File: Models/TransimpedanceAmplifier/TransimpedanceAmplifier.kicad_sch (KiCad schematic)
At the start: 1 part, among them U1 Teensy4.1

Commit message: Filled in some detail
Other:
- removed sheet TIA_1Stage
- removed sheet TIA_2Stage
- added sheet TIA_OneStage (TIA_OneStage.kicad_sch)
- added sheet TIA_TwoStage (TIA_TwoStage.kicad_sch)
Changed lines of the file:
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@@
+	)
+	(sheet
+		(at 233.68 60.96)
+		(size 35.56 25.4)
+		(exclude_from_sim no)
+		(in_bom yes)
+		(on_board yes)
+		(dnp no)
+		(fields_autoplaced yes)
+		(stroke
+			(width 0.1524)
+			(type solid)
+		)
+		(fill
+			(color 0 0 0 0.0000)
+		)
+		(property "Sheetname" "TIA_TwoStage"
+			(at 233.68 60.2484 0)
+			(effects
+				(font
+					(size 1.27 1.27)
+				)
+				(justify left bottom)
+			)
+		)
+		(property "Sheetfile" "TIA_TwoStage.kicad_sch"
+			(at 233.68 86.9446 0)
+			(effects
+				(font
+					(size 1.27 1.27)
+				)
+				(justify left top)
+			)
+		)
+		(instances
+			(project "TransimpedanceAmplifier"
+				(path "/ec9f2ae3-e40d-40eb-9760-2b611ee8efd1"
+					(page "7")
+				)
+			)
+		)
 	)
 	(sheet
@@
 	)
 	(sheet
-		(at 231.14 25.4)
-		(size 35.56 25.4)
-		(exclude_from_sim no)
-		(in_bom yes)
-		(on_board yes)
-		(dnp no)
-		(fields_autoplaced yes)
-		(stroke
-			(width 0.1524)
-			(type solid)
-		)
-		(fill
-			(color 0 0 0 0.0000)
-		)
-		(property "Sheetname" "TIA_1Stage"
-			(at 231.14 24.6884 0)
-			(effects
-				(font
-					(size 1.27 1.27)
-				)
-				(justify left bottom)
-			)
-		)
-		(property "Sheetfile" "TIA_1Stage.kicad_sch"
-			(at 231.14 51.3846 0)
-			(effects
-				(font
-					(size 1.27 1.27)
-				)
-				(justify left top)
-			)
-		)
-		(instances
-			(project "TransimpedanceAmplifier"
-				(path "/ec9f2ae3-e40d-40eb-9760-2b611ee8efd1"
-					(page "6")
-				)
-			)
-		)
-	)
-	(sheet
-		(at 231.14 63.5)
-		(size 35.56 22.86)
-		(exclude_from_sim no)
-		(in_bom yes)
-		(on_board yes)
-		(dnp no)
-		(fields_autoplaced yes)
-		(stroke
-			(width 0.1524)
-			(type solid)
-		)
-		(fill
-			(color 0 0 0 0.0000)
-		)
-		(property "Sheetname" "TIA_2Stage"
-			(at 231.14 62.7884 0)
-			(effects
-				(font
-					(size 1.27 1.27)
-				)
-				(justify left bottom)
-			)
-		)
-		(property "Sheetfile" "TIA_2Stage.kicad_sch"
-			(at 231.14 86.9446 0)
-			(effects
-				(font
-					(size 1.27 1.27)
-				)
-				(justify left top)
-			)
-		)
-		(instances
-			(project "TransimpedanceAmplifier"
-				(path "/ec9f2ae3-e40d-40eb-9760-2b611ee8efd1"
-					(page "7")
-				)
-			)
-		)
-	)
-	(sheet
 		(at 27.94 132.08)
 		(size 33.02 25.4)
@@
 				)
 			)
+		)
+	)
+	(sheet
+		(at 233.68 25.4)
+		(size 35.56 25.4)
+		(exclude_from_sim no)
+		(in_bom yes)
+		(on_board yes)
+		(dnp no)
+		(fields_autoplaced yes)
+		(stroke
+			(width 0.1524)
+			(type solid)
+		)
+		(fill
+			(color 0 0 0 0.0000)
+		)
+		(property "Sheetname" "TIA_OneStage"
+			(at 233.68 24.6884 0)
+			(effects
+				(font
+					(size 1.27 1.27)
+				)
+				(justify left bottom)
+			)
+		)
+		(property "Sheetfile" "TIA_OneStage.kicad_sch"
+			(at 233.68 51.3846 0)
+			(effects
+				(font
+					(size 1.27 1.27)
+				)
+				(justify left top)
+			)
+		)
+		(instances
+			(project "TransimpedanceAmplifier"
+				(path "/ec9f2ae3-e40d-40eb-9760-2b611ee8efd1"
+					(page "6")
+				)
+			)

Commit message: Save progress
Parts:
- removed U1: Teensy4.1, symbol teensy:Teensy4.1
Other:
- added sheet Teensy (Teensy.kicad_sch)
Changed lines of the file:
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@@
 	(generator_version "9.0")
 	(paper "A4")
-	(symbol
-		(lib_id "teensy:Teensy4.1")
-		(at 144.78 111.76 0)
-		(unit 1)
-		(exclude_from_sim no)
-		(in_bom yes)
-		(on_board yes)
-		(dnp no)
-		(fields_autoplaced yes)
-		(property "Reference" "U1"
-			(at 144.78 45.72 0)
-			(effects
-				(font
-					(size 1.27 1.27)
-				)
-			)
-		)
-		(property "Value" "Teensy4.1"
-			(at 144.78 48.26 0)
-			(effects
-				(font
-					(size 1.27 1.27)
-				)
-			)
-		)
-		(property "Footprint" ""
-			(at 134.62 101.6 0)
-			(effects
-				(font
-					(size 1.27 1.27)
-				)
-				(hide yes)
-			)
-		)
-		(property "Datasheet" ""
-			(at 134.62 101.6 0)
-			(effects
-				(font
-					(size 1.27 1.27)
-				)
-				(hide yes)
-			)
-		)
-		(property "Description" ""
-			(at 144.78 111.76 0)
-			(effects
-				(font
-					(size 1.27 1.27)
-				)
-				(hide yes)
-			)
-		)
-		(pin "5"
-		)
-		(pin "6"
-		)
-		(pin "7"
-		)
-		(pin "8"
-		)
-		(pin "9"
-		)
-		(pin "10"
-		)
-		(pin "11"
-		)
-		(pin "12"
-		)
-		(pin "13"
-		)
-		(pin "14"
-		)
-		(pin "15"
-		)
-		(pin "16"
-		)
-		(pin "17"
-		)
-		(pin "18"
-		)
-		(pin "19"
-		)
-		(pin "20"
-		)
-		(pin "21"
-		)
-		(pin "22"
-		)
-		(pin "23"
-		)
-		(pin "24"
-		)
-		(pin "66"
-		)
-		(pin "67"
-		)
-		(pin "55"
-		)
-		(pin "56"
-		)
-		(pin "57"
-		)
-		(pin "58"
-		)
-		(pin "59"
-		)
-		(pin "50"
-		)
-		(pin "51"
-		)
-		(pin "52"
-		)
-		(pin "53"
-		)
-		(pin "54"
-		)
-		(pin "49"
-		)
-		(pin "48"
-		)
-		(pin "47"
-		)
-		(pin "46"
-		)
-		(pin "45"
-		)
-		(pin "44"
-		)
-		(pin "43"
-		)
-		(pin "42"
-		)
-		(pin "41"
-		)
-		(pin "40"
-		)
-		(pin "39"
-		)
-		(pin "38"
-		)
-		(pin "37"
-		)
-		(pin "36"
-		)
-		(pin "35"
-		)
-		(pin "33"
-		)
-		(pin "32"
-		)
-		(pin "31"
-		)
-		(pin "30"
-		)
-		(pin "29"
-		)
-		(pin "28"
-		)
-		(pin "27"
-		)
-		(pin "26"
-		)
-		(pin "25"
-		)
-		(pin "65"
-		)
-		(pin "64"
-		)
-		(pin "63"
-		)
-		(pin "62"
-		)
-		(pin "61"
-		)
-		(pin "60"
-		)
-		(pin "1"
-		)
-		(pin "2"
-		)
-		(pin "3"
-		)
-		(pin "4"
-		)
-		(pin "34"
-		)
-		(instances
-			(project ""
-				(path "/ec9f2ae3-e40d-40eb-9760-2b611ee8efd1"
-					(reference "U1")
-					(unit 1)
-				)
-			)
-		)
-	)
 	(sheet
 		(at 233.68 60.96)
@@
 				)
 			)
+		)
+	)
+	(sheet
+		(at 233.68 96.52)
+		(size 35.56 25.4)
+		(exclude_from_sim no)
+		(in_bom yes)
+		(on_board yes)
+		(dnp no)
+		(fields_autoplaced yes)
+		(stroke
+			(width 0.1524)
+			(type solid)
+		)
+		(fill
+			(color 0 0 0 0.0000)
+		)
+		(property "Sheetname" "Teensy"
+			(at 233.68 95.8084 0)
+			(effects
+				(font
+					(size 1.27 1.27)
+				)
+				(justify left bottom)
+			)
+		)
+		(property "Sheetfile" "Teensy.kicad_sch"
+			(at 233.68 122.5046 0)
+			(effects
+				(font
+					(size 1.27 1.27)
+				)
+				(justify left top)
+			)
+		)
+		(instances
+			(project "TransimpedanceAmplifier"
+				(path "/ec9f2ae3-e40d-40eb-9760-2b611ee8efd1"
+					(page "10")
+				)
+			)

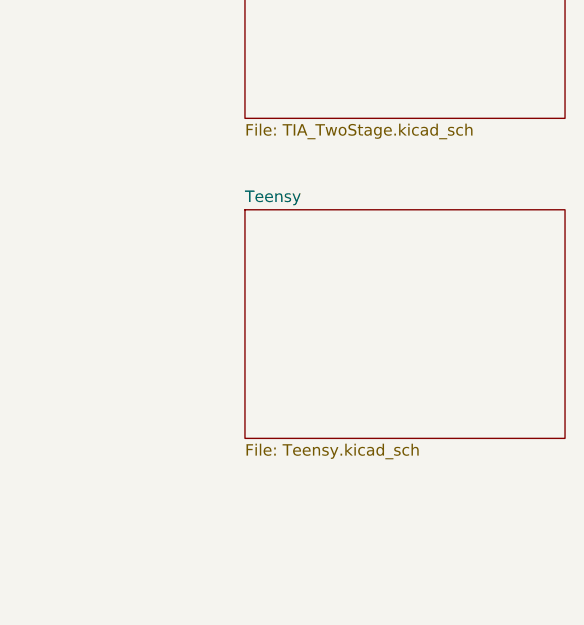
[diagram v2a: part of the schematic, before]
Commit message: Assigned all the SPI pins
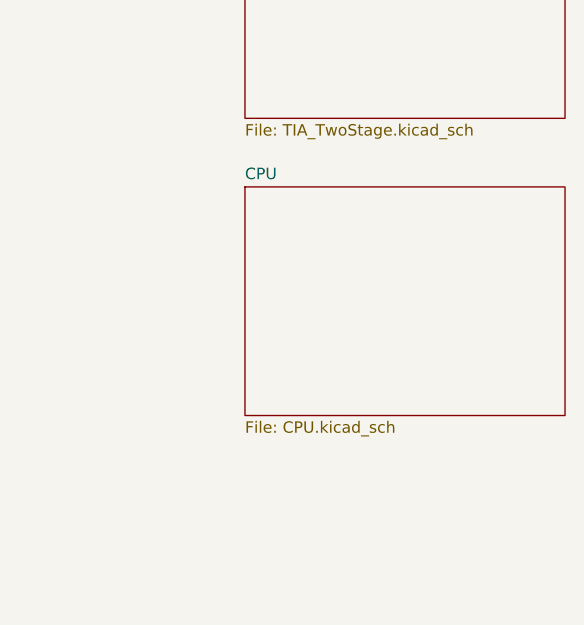
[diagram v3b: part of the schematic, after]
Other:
- removed sheet Teensy
- added sheet CPU (CPU.kicad_sch)
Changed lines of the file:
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@@
 	)
 	(sheet
-		(at 233.68 96.52)
+		(at 233.68 93.98)
 		(size 35.56 25.4)
 		(exclude_from_sim no)
@@
 			(color 0 0 0 0.0000)
 		)
-		(property "Sheetname" "Teensy"
-			(at 233.68 95.8084 0)
+		(property "Sheetname" "CPU"
+			(at 233.68 93.2684 0)
 			(effects
 				(font
@@
 			)
 		)
-		(property "Sheetfile" "Teensy.kicad_sch"
-			(at 233.68 122.5046 0)
+		(property "Sheetfile" "CPU.kicad_sch"
+			(at 233.68 119.9646 0)
 			(effects
 				(font
@@
 			(project "TransimpedanceAmplifier"
 				(path "/ec9f2ae3-e40d-40eb-9760-2b611ee8efd1"
-					(page "10")
+					(page "16")
 				)
 			)

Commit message: Save progress
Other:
- note added: "Mechanical switch to choose which TIA the current goes to and/or which TIA output voltage is read by the ADC. Unknown how this would be implemented (perhaps swapping out entire circuit boards?) Abstract away the DUT + TIA1 + TIA2 into a hierarchical sheet that just accepts input and output voltage."
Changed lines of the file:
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@@
 	(generator_version "9.0")
 	(paper "A4")
-	(sheet
-		(at 233.68 60.96)
+	(text "Mechanical switch to choose which TIA the current goes to\nand/or which TIA output voltage is read by the ADC.\nUnknown how this would be implemented (perhaps swapping\nout entire circuit boards?)\n\nAbstract away the DUT + TIA1 + TIA2 into a hierarchical\nsheet that just accepts input and output voltage."
+		(exclude_from_sim no)
+		(at 110.49 170.434 0)
+		(effects
+			(font
+				(size 1.27 1.27)
+			)
+			(justify left)
+		)
+	)
+	(sheet
+		(at 139.7 128.27)
 		(size 35.56 25.4)
 		(exclude_from_sim no)
@@
 		)
 		(property "Sheetname" "TIA_TwoStage"
-			(at 233.68 60.2484 0)
+			(at 139.7 127.5584 0)
 			(effects
 				(font
@@
 		)
 		(property "Sheetfile" "TIA_TwoStage.kicad_sch"
-			(at 233.68 86.9446 0)
+			(at 139.7 154.2546 0)
 			(effects
 				(font
@@
 	)
 	(sheet
-		(at 27.94 60.96)
+		(at 187.96 106.68)
 		(size 33.02 25.4)
 		(exclude_from_sim no)
@@
 		)
 		(property "Sheetname" "ADC"
-			(at 27.94 60.2484 0)
+			(at 187.96 105.9684 0)
 			(effects
 				(font
@@
 		)
 		(property "Sheetfile" "ADC.kicad_sch"
-			(at 27.94 86.9446 0)
+			(at 187.96 132.6646 0)
 			(effects
 				(font
@@
 	)
 	(sheet
-		(at 27.94 25.4)
+		(at 55.88 109.22)
 		(size 33.02 25.4)
 		(exclude_from_sim no)
@@
 		)
 		(property "Sheetname" "DAC"
-			(at 27.94 24.6884 0)
+			(at 55.88 108.5084 0)
 			(effects
 				(font
@@
 		)
 		(property "Sheetfile" "DAC.kicad_sch"
-			(at 27.94 51.3846 0)
+			(at 55.88 135.2046 0)
 			(effects
 				(font
@@
 	)
 	(sheet
-		(at 27.94 96.52)
+		(at 151.13 31.75)
 		(size 33.02 25.4)
 		(exclude_from_sim no)
@@
 		)
 		(property "Sheetname" "Power"
-			(at 27.94 95.8084 0)
+			(at 151.13 31.0384 0)
 			(effects
 				(font
@@
 		)
 		(property "Sheetfile" "Power.kicad_sch"
-			(at 27.94 122.5046 0)
+			(at 151.13 57.7346 0)
 			(effects
 				(font
@@
 	)
 	(sheet
-		(at 233.68 93.98)
+		(at 95.25 31.75)
 		(size 35.56 25.4)
 		(exclude_from_sim no)
@@
 		)
 		(property "Sheetname" "CPU"
-			(at 233.68 93.2684 0)
+			(at 95.25 31.0384 0)
 			(effects
 				(font
@@
 		)
 		(property "Sheetfile" "CPU.kicad_sch"
-			(at 233.68 119.9646 0)
+			(at 95.25 57.7346 0)
 			(effects
 				(font
@@
 	)
 	(sheet
-		(at 27.94 132.08)
+		(at 97.79 109.22)
 		(size 33.02 25.4)
 		(exclude_from_sim no)
@@
 		)
 		(property "Sheetname" "DUT"
-			(at 27.94 131.3684 0)
+			(at 97.79 108.5084 0)
 			(effects
 				(font
@@
 		)
 		(property "Sheetfile" "DUT.kicad_sch"
-			(at 27.94 158.0646 0)
+			(at 97.79 135.2046 0)
 			(effects
 				(font
@@
 	)
 	(sheet
-		(at 233.68 25.4)
+		(at 139.7 88.9)
 		(size 35.56 25.4)
 		(exclude_from_sim no)
@@
 		)
 		(property "Sheetname" "TIA_OneStage"
-			(at 233.68 24.6884 0)
+			(at 139.7 88.1884 0)
 			(effects
 				(font
@@
 		)
 		(property "Sheetfile" "TIA_OneStage.kicad_sch"
-			(at 233.68 51.3846 0)
-			(effects
-				(font
+			(at 139.7 114.8846 0)
+			(effects
+				(font

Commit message: Save progress
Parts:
- added SW1: SW_SPDT, symbol Switch:SW_SPDT
- added SW2: SW_SPDT_312, symbol Switch:SW_SPDT_312
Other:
- note added: "TODO: Investigate effects of the switch on leakage current, when placed between the DUT and the TIA"
- note added: "TODO: Merge DAC and ADC into CPU module"
- note removed: "Mechanical switch to choose which TIA the current goes to and/or which TIA output voltage is read by the ADC. Unknown how this would be implemented (perhaps swapping out entire circuit boards?) Abstract away the DUT + TIA1 + TIA2 into a hierarchical sheet that just accepts input and output voltage."

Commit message: Save progress after a major refactoring
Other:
- removed sheet ADC
- removed sheet DAC
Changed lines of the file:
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@@
-	)
-	(sheet
-		(at 63.5 59.69)
-		(size 33.02 25.4)
-		(exclude_from_sim no)
-		(in_bom yes)
-		(on_board yes)
-		(dnp no)
-		(fields_autoplaced yes)
-		(stroke
-			(width 0.1524)
-			(type solid)
-		)
-		(fill
-			(color 0 0 0 0.0000)
-		)
-		(property "Sheetname" "ADC"
-			(at 63.5 58.9784 0)
-			(effects
-				(font
-					(size 1.27 1.27)
-				)
-				(justify left bottom)
-			)
-		)
-		(property "Sheetfile" "ADC.kicad_sch"
-			(at 63.5 85.6746 0)
-			(effects
-				(font
-					(size 1.27 1.27)
-				)
-				(justify left top)
-			)
-		)
-		(instances
-			(project "TransimpedanceAmplifier"
-				(path "/ec9f2ae3-e40d-40eb-9760-2b611ee8efd1"
-					(page "3")
-				)
-			)
-		)
-	)
-	(sheet
-		(at 25.4 60.96)
-		(size 33.02 25.4)
-		(exclude_from_sim no)
-		(in_bom yes)
-		(on_board yes)
-		(dnp no)
-		(fields_autoplaced yes)
-		(stroke
-			(width 0.1524)
-			(type solid)
-		)
-		(fill
-			(color 0 0 0 0.0000)
-		)
-		(property "Sheetname" "DAC"
-			(at 25.4 60.2484 0)
-			(effects
-				(font
-					(size 1.27 1.27)
-				)
-				(justify left bottom)
-			)
-		)
-		(property "Sheetfile" "DAC.kicad_sch"
-			(at 25.4 86.9446 0)
-			(effects
-				(font
-					(size 1.27 1.27)
-				)
-				(justify left top)
-			)
-		)
-		(instances
-			(project "TransimpedanceAmplifier"
-				(path "/ec9f2ae3-e40d-40eb-9760-2b611ee8efd1"
-					(page "2")
-				)
-			)
-		)
 	)
 	(sheet

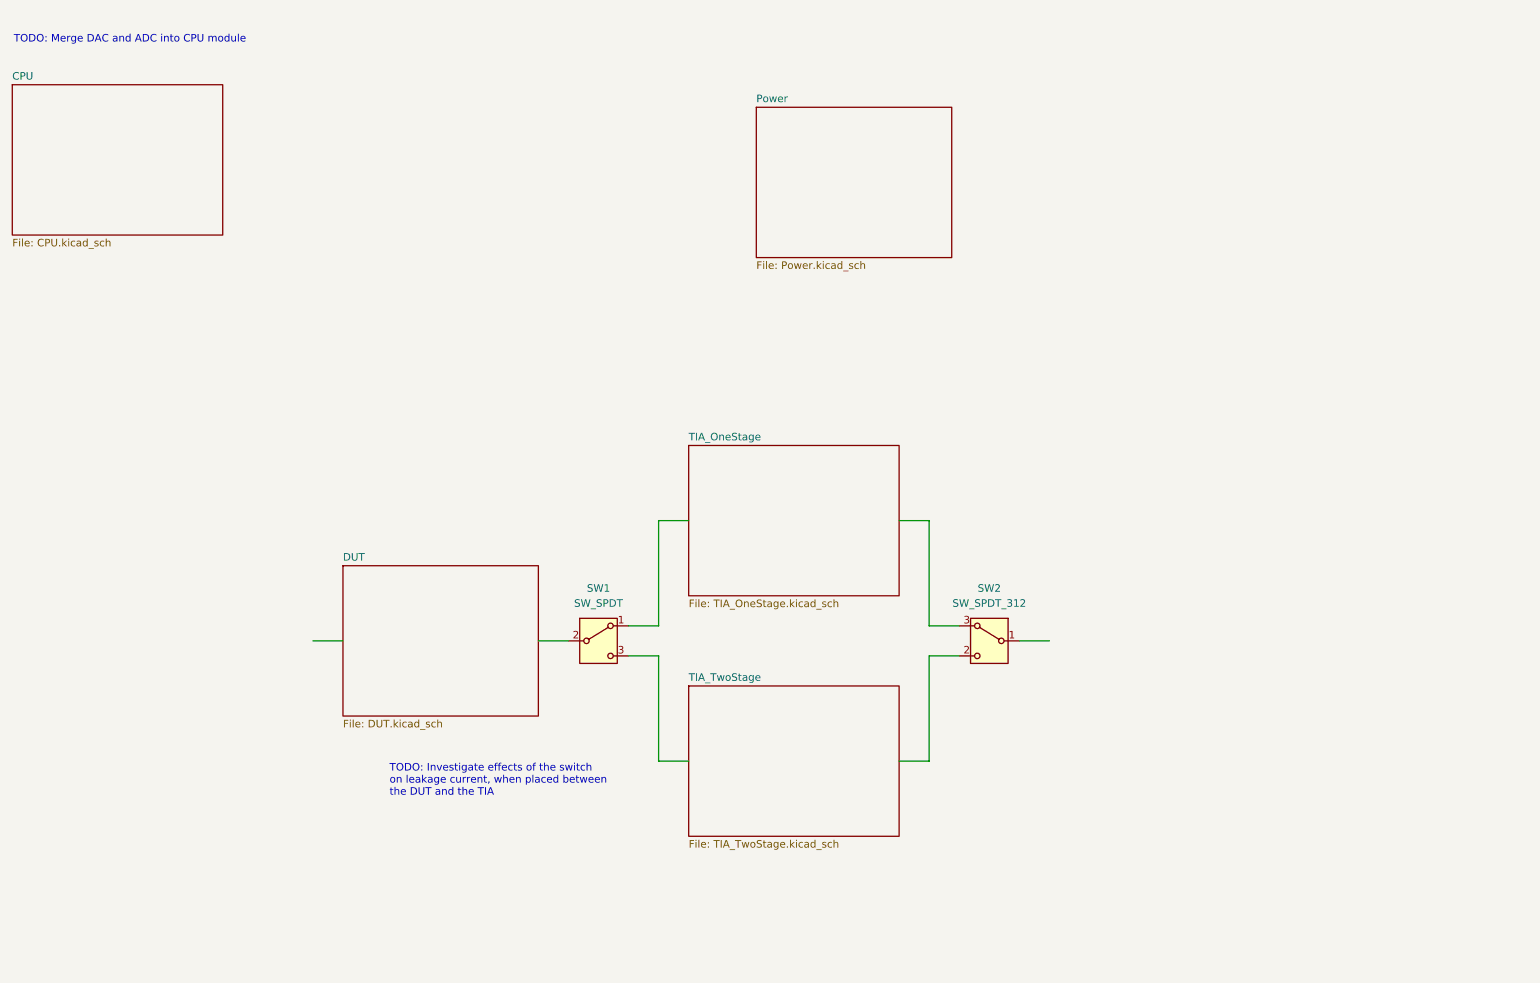
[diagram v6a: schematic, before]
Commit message: Fully specified the high-level connections between subsystems
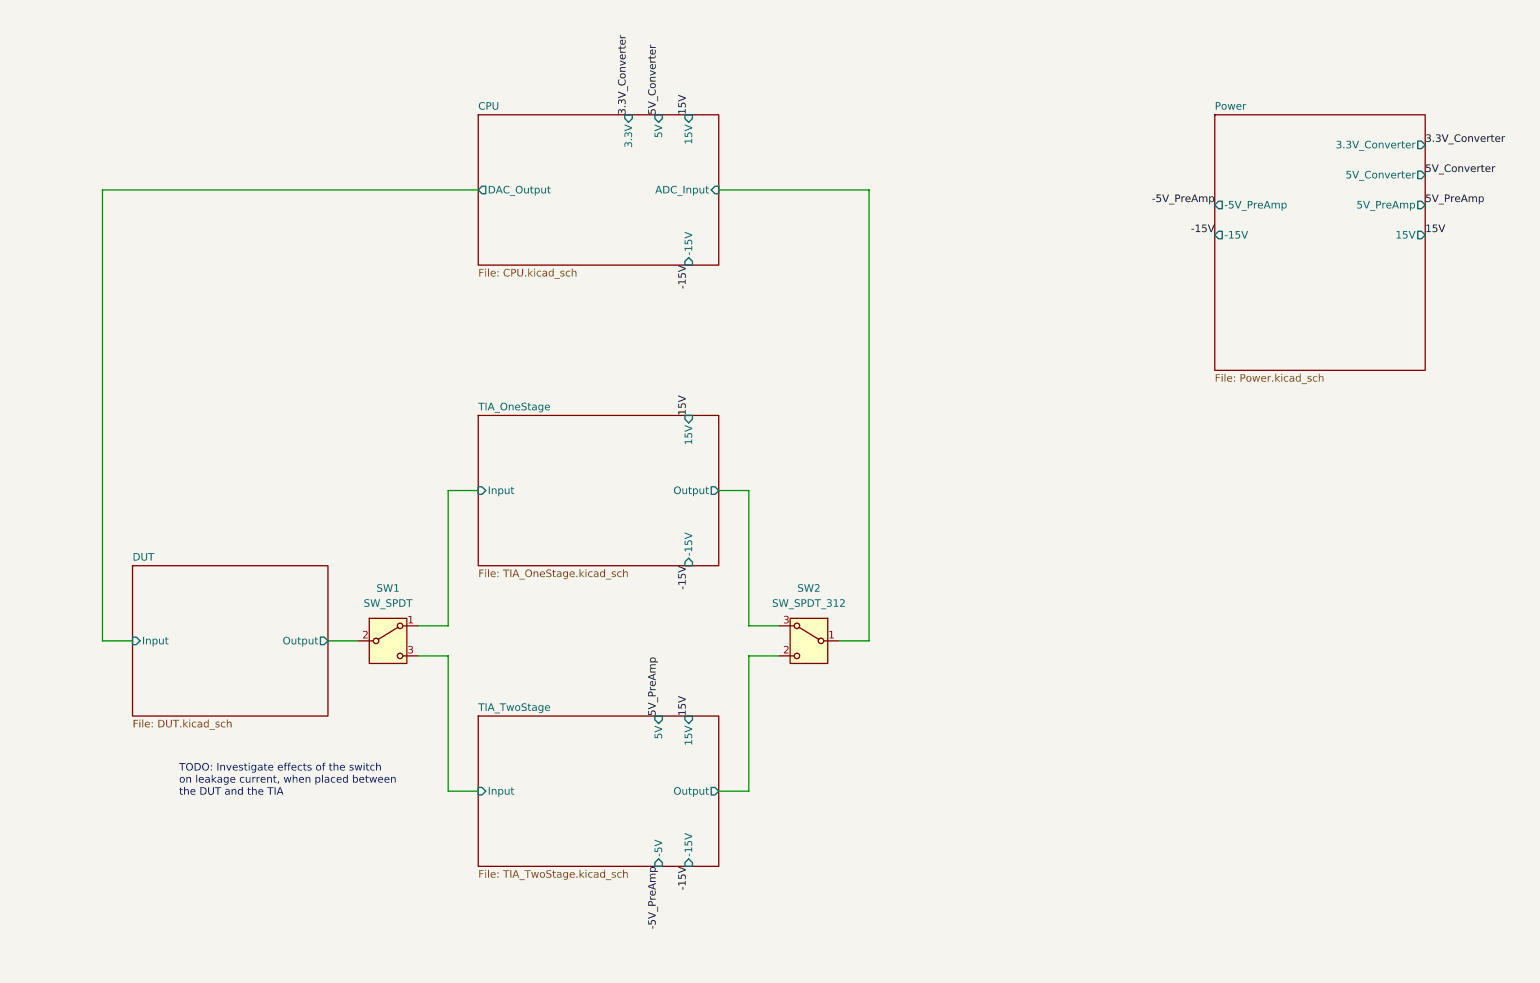
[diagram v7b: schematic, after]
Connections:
- net TIA_OneStage/Input: now reaches SW1.1 (A)
- net DUT/Output: now reaches SW1.2 (B)
- net TIA_TwoStage/Input: now reaches SW1.3 (C)
- net CPU/ADC_Input: now reaches SW2.1 (B)
- net TIA_TwoStage/Output: now reaches SW2.2 (C)
- net TIA_OneStage/Output: now reaches SW2.3 (A)
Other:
- sheet CPU ports: added -15V, 15V, 3.3V, 5V, ADC_Input, DAC_Output; removed none
- sheet DUT ports: added Input, Output; removed none
- sheet Power ports: added -15V, -5V_PreAmp, 15V, 3.3V_Converter, 5V_Converter, 5V_PreAmp; removed none
- sheet TIA_OneStage ports: added -15V, 15V, Input, Output; removed none
- sheet TIA_TwoStage ports: added -15V, -5V, 15V, 5V, Input, Output; removed none
- note removed: "TODO: Merge DAC and ADC into CPU module"
- moved on the sheet: SW1, SW2

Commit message: Save progress
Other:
- note added: "TODO: Limit current of bias voltage supply to <5 mA to prevent damage to AD8615"
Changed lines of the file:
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@@
 	(generator_version "9.0")
 	(paper "A4")
+	(text "TODO: Limit current of bias voltage supply\nto <5 mA to prevent damage to AD8615"
+		(exclude_from_sim no)
+		(at 45.974 51.562 0)
+		(effects
+			(font
+				(size 1.27 1.27)
+			)
+			(justify left top)
+		)
+	)
 	(text "TODO: Investigate effects of the switch\non leakage current, when placed between\nthe DUT and the TIA"
 		(exclude_from_sim no)
